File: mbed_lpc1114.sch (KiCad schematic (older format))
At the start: 23 parts

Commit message: パラメータ調整
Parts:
- added 1uF: C, 10uF, symbol C
- added C7: 1uF, symbol C
- added D1: LED, symbol LED
- added R8: 330, symbol R
- added U1: lpc1114fn28, symbol lpc1114fn28
- C1: renamed from C?; value C -> 0.1
- C2, C5: renamed from C?; value CP -> 100uF
- C3, C4: renamed from C?; value C -> 0.1uF
- C8, C9: renamed from C?; value C -> 1uF
- R1: renamed from R?; value R -> 1.5k
- R2, R3: renamed from R?; value R -> 27
- R4, R5: renamed from R?; value R -> 10k
- R6, R7: renamed from R?; value R -> 1k
- gave numbers to parts that had none: 9
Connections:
- wire segments 60 -> 214
- no-connect marks 0 -> 6
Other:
- moved on the sheet: C2, C3, C4, C5, C8, C9, J1, R4, R5, R6, R7, U3

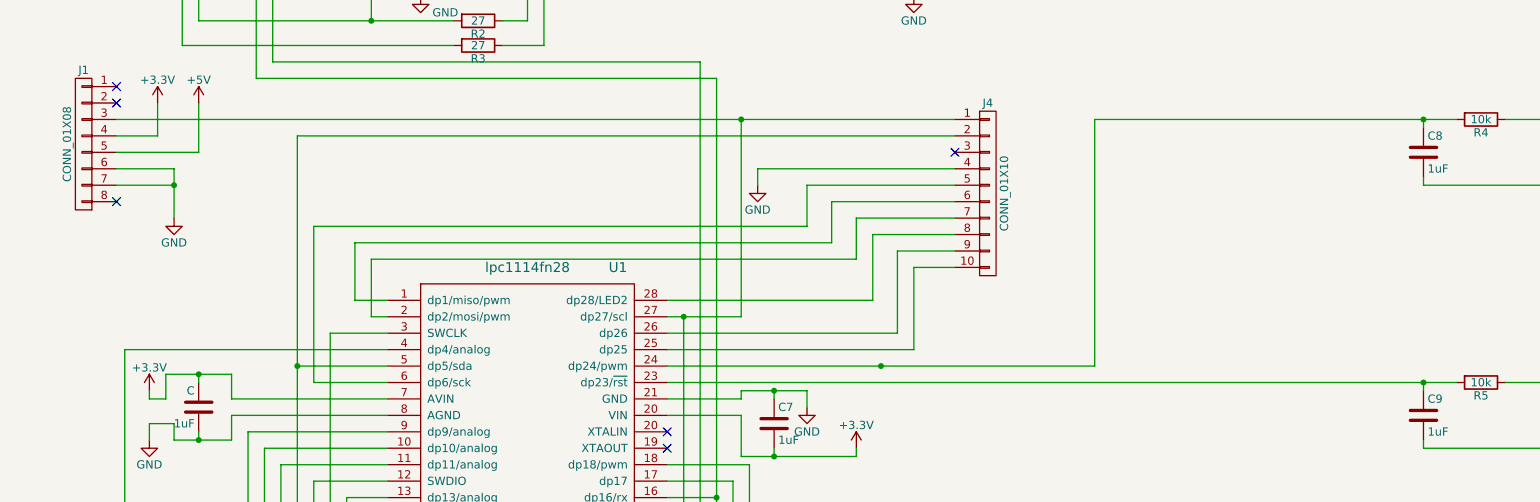
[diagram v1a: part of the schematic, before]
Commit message: リセットピン修正
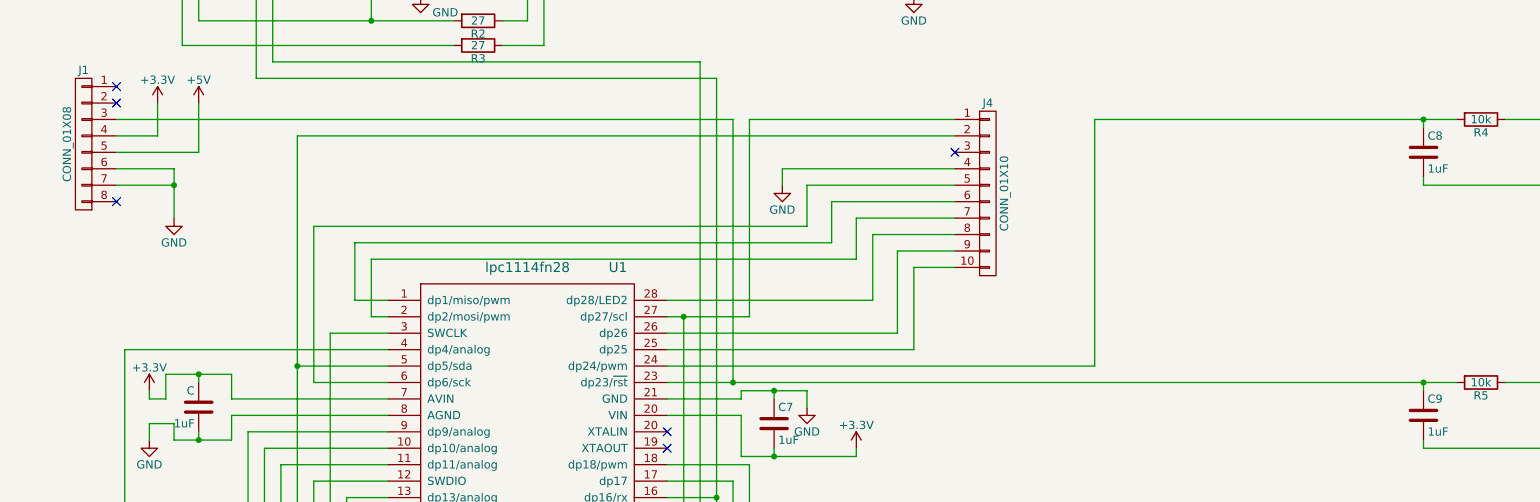
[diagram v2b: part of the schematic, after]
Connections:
- net at J2.6 (P6), J4.1 (P1), U1.27 (dp27/scl): no longer J1.3 (P3)
- net at C9.1, R5.2, U1.23 (dp23/~rst): now also J1.3 (P3)
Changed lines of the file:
@@
 L GND #PWR019
 U 1 1 5904C964
-P 5700 3300
-F 0 "#PWR019" H 5700 3050 50  0001 C CNN
-F 1 "GND" H 5700 3150 50  0000 C CNN
-F 2 "" H 5700 3300 50  0001 C CNN
-F 3 "" H 5700 3300 50  0001 C CNN
-	1    5700 3300
+P 5850 3300
+F 0 "#PWR019" H 5850 3050 50  0001 C CNN
+F 1 "GND" H 5850 3150 50  0000 C CNN
+F 2 "" H 5850 3300 50  0001 C CNN
+F 3 "" H 5850 3300 50  0001 C CNN
+	1    5850 3300
 	1    0    0    -1
 $EndComp
@@
 	10600 3850 10600 4050
 Wire Wire Line
-	5150 4500 9750 4500
+	5150 4500 5550 4500
+Wire Wire Line
+	5550 4500 9750 4500
 Wire Wire Line
 	9750 4500 9950 4500
@@
 Connection ~ 2300 4850
 Wire Wire Line
-	1800 2900 5600 2900
-Wire Wire Line
-	5600 2900 6900 2900
+	5650 2900 6900 2900
 Wire Wire Line
 	2050 2800 2050 3000
@@
 	5650 5000 5150 5000
 Wire Wire Line
-	5150 4400 6450 4400
-Wire Wire Line
-	6450 4400 7750 4400
+	5150 4400 7750 4400
 Wire Wire Line
 	3200 5950 6950 5950
@@
 	5150 4100 5250 4100
 Wire Wire Line
-	5250 4100 5600 4100
+	5250 4100 5650 4100
 Connection ~ 2900 4400
-Connection ~ 5600 2900
 Wire Wire Line
 	2900 3000 6900 3000
 Wire Wire Line
-	6900 3200 5700 3200
-Wire Wire Line
-	5700 3200 5700 3300
+	6900 3200 5850 3200
+Wire Wire Line
+	5850 3200 5850 3300
 Wire Wire Line
 	6900 3300 6000 3300
@@
 	8050 5350 8050 5500
 Connection ~ 6850 5850
-Connection ~ 6450 4400
 Wire Wire Line
 	3450 5100 3000 5100
@@
 NoConn ~ 6900 3100
 Wire Wire Line
-	5600 4100 5600 2900
+	5650 4100 5650 2900
 Connection ~ 5250 4100
 Wire Wire Line
@@
 Wire Wire Line
 	3650 2150 3650 2100
+Wire Wire Line
+	1800 2900 5550 2900
+Wire Wire Line
+	5550 2900 5550 4500
+Connection ~ 5550 4500
 $EndSCHEMATC

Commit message: ライブラリ修正
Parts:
- removed U1: lpc1114fn28, symbol lpc1114fn28
- added U?: lpc1114fn28, symbol lpc1114fn28
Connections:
- net +3V3: now also U?.20 (XTALIN), U?.7 (AVIN)
- net GND: now also U?.21 (GND), U?.8 (AGND)
- net at C9.1, J1.3 (P3), R5.2: now also U?.23 (dp23/~rst)
- net at J2.1 (P1): now also U?.4 (dp4/analog)
- net at J2.2 (P2): now also U?.9 (dp9/analog)
- net at J2.3 (P3): now also U?.10 (dp10/analog)
- net at J2.4 (P4): now also U?.11 (dp11/analog)
- net at J2.5 (P5), J4.2 (P2): now also U?.5 (dp5/sda)
- net at J2.6 (P6), J4.1 (P1): now also U?.27 (dp27/scl)
- net at J4.10 (P10): now also U?.25 (dp25)
- net at J4.5 (P5): now also U?.6 (dp6/sck)
- net at J4.6 (P6): now also U?.1 (dp1/miso/pwm)
- net at J4.7 (P7): now also U?.2 (dp2/mosi/pwm)
- net at J4.8 (P8): now also U?.28 (dp28/LED2)
- net at J4.9 (P9): now also U?.26 (dp26)
- net at J3.1 (P1): now also U?.3 (SWCLK)
- net at J3.2 (P2): now also U?.12 (SWDIO)
- net at D1.2 (A), J3.3 (P3): now also U?.14 (dp14/LED1)
- net at J3.4 (P4): now also U?.13 (dp13/analog)
- net at J3.5 (P5): now also U?.18 (dp18/pwm)
- net at J3.6 (P6): now also U?.17 (dp17)
- net at J3.7 (P7), U2.4 (RXD): now also U?.15 (dp15/tx)
- net at J3.8 (P8), U2.2 (TXD): now also U?.16 (dp16/rx)
- net at C8.1, R4.2: now also U?.24 (dp24/pwm)
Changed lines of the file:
@@
 LIBS:switch
 LIBS:lpc1114fn28
-LIBS:mbed_lpc1114-cache
 EELAYER 25 0
 EELAYER END
@@
 $EndComp
 $Comp
-L lpc1114fn28 U1
-U 1 1 5904BE70
-P 4300 4650
-F 0 "U1" H 4850 5500 60  0000 C CNN
-F 1 "lpc1114fn28" H 4300 5500 60  0000 C CNN
-F 2 "" H 4300 4650 60  0001 C CNN
-F 3 "" H 4300 4650 60  0001 C CNN
-	1    4300 4650
-	1    0    0    -1
-$EndComp
-$Comp
 L GND #PWR019
 U 1 1 5904C964
@@
 	5550 2900 5550 4500
 Connection ~ 5550 4500
+$Comp
+L lpc1114fn28 U?
+U 1 1 5904732E
+P 4300 4650
+F 0 "U?" H 4850 5500 60  0000 C CNN
+F 1 "lpc1114fn28" H 4300 5500 60  0000 C CNN
+F 2 "" H 4300 4650 60  0001 C CNN
+F 3 "" H 4300 4650 60  0001 C CNN
+	1    4300 4650
+	1    0    0    -1
+$EndComp
 $EndSCHEMATC

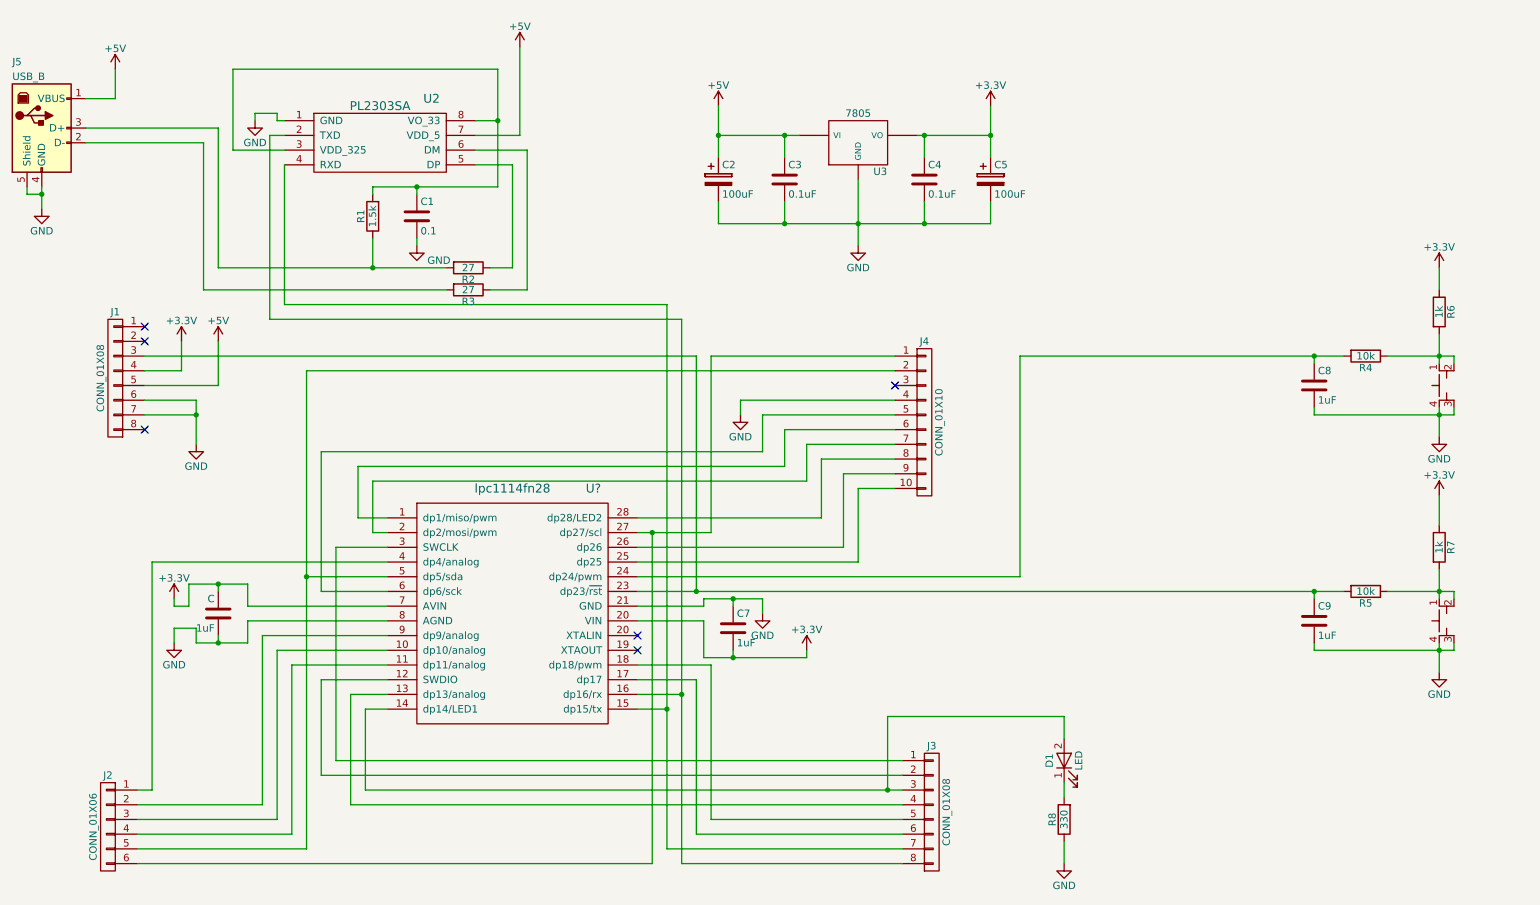
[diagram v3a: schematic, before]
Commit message: ピン配置を修正
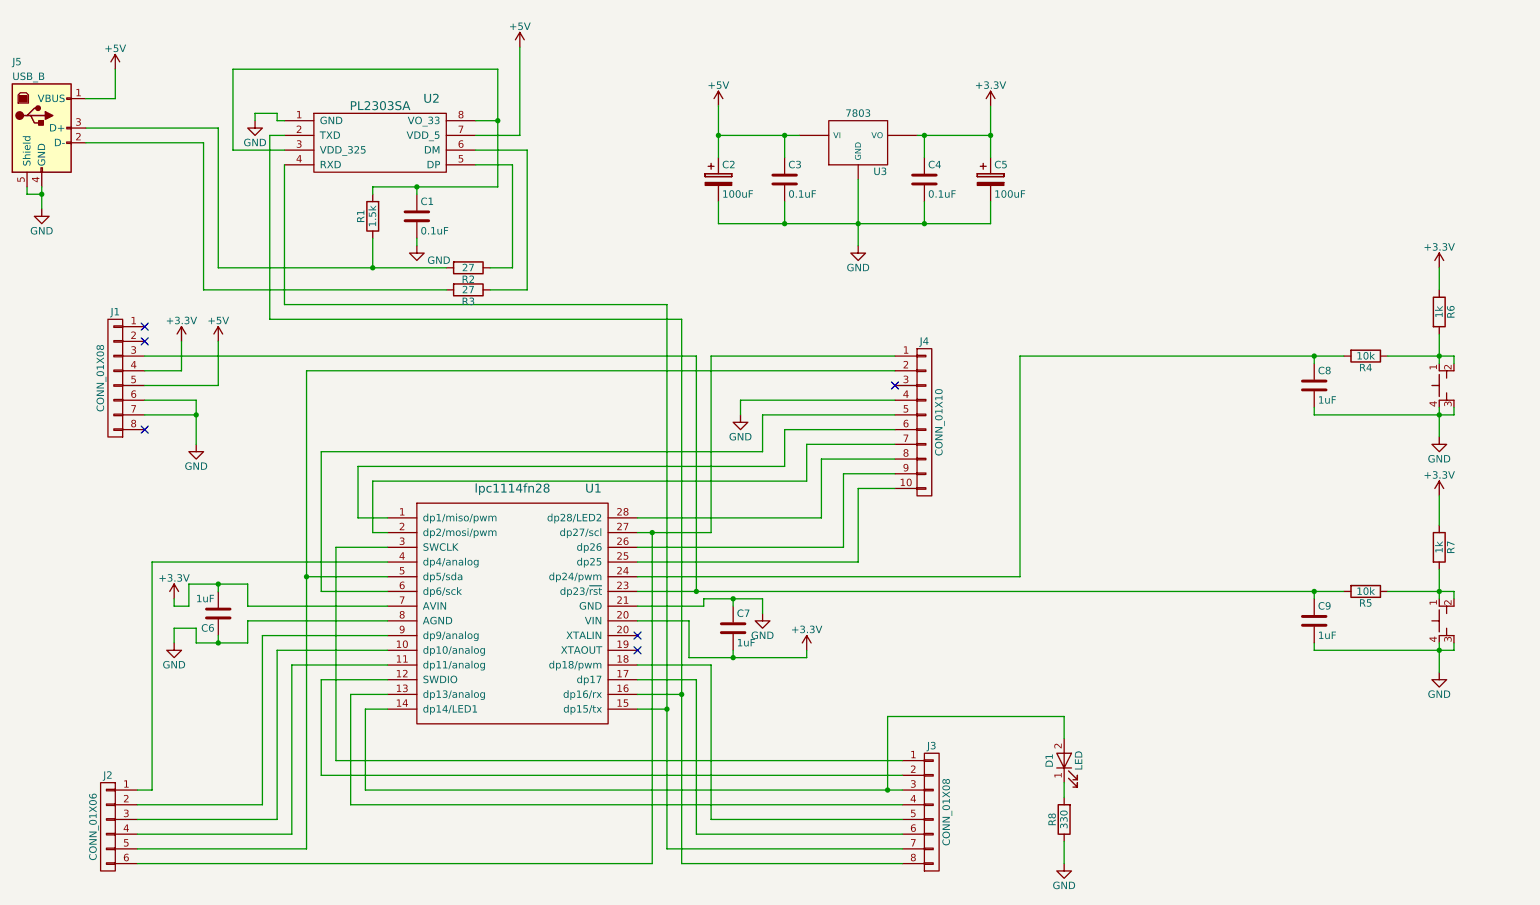
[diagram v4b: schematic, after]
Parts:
- C1: value 0.1 -> 0.1uF; footprint (none) -> Capacitors_THT:C_Disc_D3.8mm_W2.6mm_P2.50mm
- C2, C5: footprint (none) -> Capacitors_THT:CP_Radial_D5.0mm_P2.50mm
- C3, C4, C7, C8, C9: footprint (none) -> Capacitors_THT:C_Disc_D3.8mm_W2.6mm_P2.50mm
- C6: renamed from 1uF; value C -> 1uF; footprint 10uF -> Capacitors_THT:C_Disc_D3.8mm_W2.6mm_P2.50mm
- D1: footprint (none) -> LEDs:LED_D3.0mm
- J1, J3: footprint (none) -> Pin_Headers:Pin_Header_Straight_1x08_Pitch2.54mm
- J2: footprint (none) -> Pin_Headers:Pin_Header_Straight_1x06_Pitch2.54mm
- J4: footprint (none) -> Pin_Headers:Pin_Header_Straight_1x10_Pitch2.54mm
- J5: footprint (none) -> Connectors:USB_B
- R1, R2, R3, R4, R5, R6, R7: footprint (none) -> Resistors_THT:R_Axial_DIN0204_L3.6mm_D1.6mm_P5.08mm_Horizontal
- R8: footprint (none) -> Resistors_THT:R_Axial_DIN0207_L6.3mm_D2.5mm_P15.24mm_Horizontal
- U1: renamed from U?; footprint (none) -> Housings_DIP:DIP-28_W15.24mm_LongPads
- U2: footprint (none) -> Housings_SOIC:SOIC-8_3.9x4.9mm_Pitch1.27mm
- U3: value 7805 -> 7803; footprint (none) -> mylib:7805
- U4, U5: footprint (none) -> Buttons_Switches_THT:SW_TH_Tactile_Omron_B3F-10xx

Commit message: 完成！
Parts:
- R8: footprint Resistors_THT:R_Axial_DIN0207_L6.3mm_D2.5mm_P15.24mm_Horizontal -> Resistors_THT:R_Axial_DIN0207_L6.3mm_D2.5mm_P10.16mm_Horizontal
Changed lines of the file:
@@
 F 0 "R8" V 8130 6050 50  0000 C CNN
 F 1 "330" V 8050 6050 50  0000 C CNN
-F 2 "Resistors_THT:R_Axial_DIN0207_L6.3mm_D2.5mm_P15.24mm_Horizontal" V 7980 6050 50  0001 C CNN
+F 2 "Resistors_THT:R_Axial_DIN0207_L6.3mm_D2.5mm_P10.16mm_Horizontal" V 7980 6050 50  0001 C CNN
 F 3 "" H 8050 6050 50  0001 C CNN
 	1    8050 6050
